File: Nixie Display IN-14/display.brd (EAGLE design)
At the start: 112.6 x 51.6 mm, 22 parts, among them U1 TPIC6B595DWRG4, U2 TPIC6B595DWRG4, U3 TPIC6B595DWRG4, U4 TPIC6B595DWRG4, U5 TPIC6B595DWRG4, X1 22-23-2021

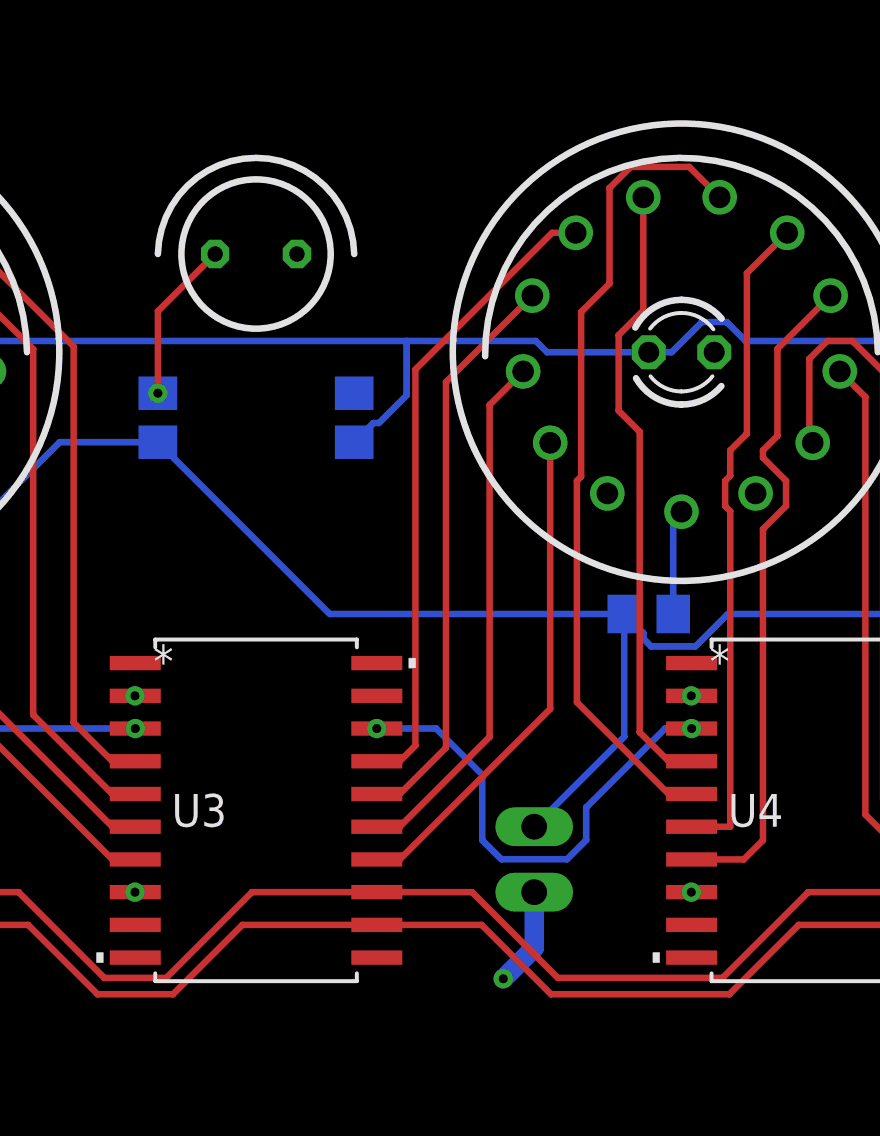
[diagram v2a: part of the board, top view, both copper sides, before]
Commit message: Reverses polarity of IN3
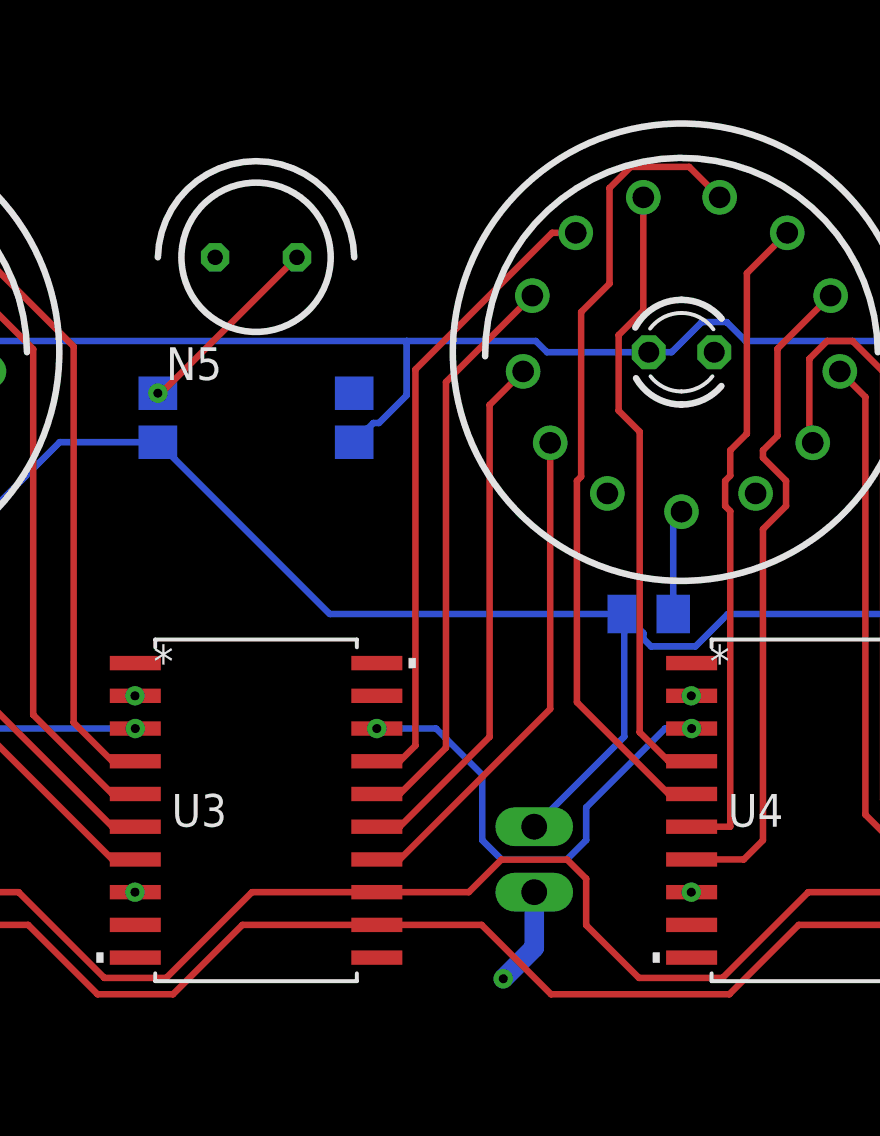
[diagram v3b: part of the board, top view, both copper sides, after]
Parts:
- moved N5 0.13 mm to (56.3, 38.1)
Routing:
- net N$49: track 109.0 -> 111.1 mm
- net N$22: track 6.32 -> 7.58 mm
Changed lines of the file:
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@@
 <setting verticaltext="up"/>
 </settings>
-<grid distance="5" unitdist="mil" unit="mil" style="lines" multiple="1" display="no" altdistance="5" altunitdist="mil" altunit="mil"/>
+<grid distance="50" unitdist="mil" unit="mil" style="lines" multiple="1" display="no" altdistance="5" altunitdist="mil" altunit="mil"/>
 <layers>
 <layer number="1" name="Top" color="4" fill="1" visible="yes" active="yes"/>
@@
 <element name="N3" library="nixies-us" package="IN-14" value="IN-14" x="72.771" y="34.417" smashed="yes"/>
 <element name="N4" library="nixies-us" package="IN-14" value="IN-14" x="96.901" y="34.417" smashed="yes"/>
-<element name="N5" library="nixies-us" package="IN-3" value="IN-3" x="56.261" y="38.227" smashed="yes"/>
 <element name="LED1" library="led" library_urn="urn:adsk.eagle:library:259" package="LED3MM" package3d_urn="urn:adsk.eagle:package:15797/1" value="" x="15.621" y="34.417" smashed="yes">
 <attribute name="POPULARITY" value="97" x="15.621" y="34.417" size="1.778" layer="27" display="off"/>
@@
 <attribute name="VALUE" x="72.136" y="17.272" locked="yes" size="1.016" layer="28" ratio="10" rot="MR270"/>
 </element>
+<element name="N5" library="nixies-us" package="IN-3" value="IN-3" x="56.261" y="38.1" smashed="yes">
+<attribute name="NAME" x="52.7685" y="33.3375" size="1.27" layer="25"/>
+</element>
 </elements>
 <signals>
@@
 <contactref element="LED2" pad="K"/>
 <contactref element="LED1" pad="K"/>
-<contactref element="N5" pad="K"/>
 <polygon width="0.254" layer="1" spacing="0.3048" orphans="yes">
 <vertex x="0" y="51.435"/>
@@
 <via x="65.853971875" y="10.100971875" extent="1-16" drill="0.35"/>
 <wire x1="67.056" y1="11.303" x2="65.853971875" y2="10.100971875" width="0.762" layer="16"/>
+<contactref element="N5" pad="K"/>
 </signal>
 <signal name="VCC">
@@
 <wire x1="62.103" y1="32.74058125" x2="62.103" y2="34.8529" width="0.254" layer="16"/>
 </signal>
-<signal name="N$22">
-<contactref element="N5" pad="A"/>
-<contactref element="R2" pad="2"/>
-<via x="52.451" y="32.827" extent="1-16" drill="0.35"/>
-<wire x1="52.451" y1="32.827" x2="52.451" y2="36.0045" width="0.254" layer="1"/>
-<wire x1="52.451" y1="36.0045" x2="54.6735" y2="38.227" width="0.254" layer="1"/>
-</signal>
 <signal name="N$23">
 <contactref element="N1" pad="A"/>
@@
 <via x="60.9473" y="19.812" extent="1-16" drill="0.35"/>
 <via x="73.1647" y="19.812" extent="1-16" drill="0.35"/>
-<wire x1="60.9473" y1="19.812" x2="63.246" y2="19.812" width="0.254" layer="16"/>
-<wire x1="63.246" y1="19.812" x2="63.24725625" y2="19.812" width="0.254" layer="16"/>
 <wire x1="72.13474375" y1="19.812" x2="73.1647" y2="19.812" width="0.254" layer="16"/>
 <wire x1="69.072" y1="16.74925625" x2="72.13474375" y2="19.812" width="0.254" layer="16"/>
-<wire x1="63.246" y1="19.812" x2="65.04" y2="18.018" width="0.254" layer="16"/>
 <wire x1="65.04" y1="15.47925625" x2="65.77925625" y2="14.74" width="0.254" layer="16"/>
 <wire x1="65.77925625" y1="14.74" x2="68.33274375" y2="14.74" width="0.254" layer="16"/>
@@
 <wire x1="65.04" y1="18.018" x2="65.04" y2="15.47925625" width="0.254" layer="16"/>
 <wire x1="69.072" y1="15.47925625" x2="69.072" y2="16.74925625" width="0.254" layer="16"/>
+<wire x1="60.9473" y1="19.812" x2="63.246" y2="19.812" width="0.254" layer="16"/>
+<wire x1="63.246" y1="19.812" x2="65.04" y2="18.018" width="0.254" layer="16"/>
 </signal>
 <signal name="N$27">
@@
 <wire x1="16.637" y1="3.81" x2="17.018" y2="4.191" width="0.254" layer="1"/>
 <wire x1="17.018" y1="9.68288125" x2="16.2687" y2="10.43218125" width="0.254" layer="1"/>
+<wire x1="67.708625" y1="9.4996" x2="74.62875" y2="9.4996" width="0.254" layer="1"/>
 <wire x1="60.9473" y1="12.192" x2="65.016225" y2="12.192" width="0.254" layer="1"/>
 <wire x1="65.016225" y1="12.192" x2="67.708625" y2="9.4996" width="0.254" layer="1"/>
-<wire x1="67.708625" y1="9.4996" x2="74.62875" y2="9.4996" width="0.254" layer="1"/>
 </signal>
 <signal name="N$49">
@@
 <wire x1="14.478" y1="10.89111875" x2="14.478" y2="4.191" width="0.254" layer="1"/>
 <wire x1="14.478" y1="4.191" x2="14.097" y2="3.81" width="0.254" layer="1"/>
-<wire x1="60.9473" y1="13.462" x2="64.64425625" y2="13.462" width="0.254" layer="1"/>
-<wire x1="64.64425625" y1="13.462" x2="67.97165625" y2="10.1346" width="0.254" layer="1"/>
-<wire x1="67.97165625" y1="10.1346" x2="74.36571875" y2="10.1346" width="0.254" layer="1"/>
+<wire x1="71.12" y1="10.1346" x2="74.36571875" y2="10.1346" width="0.254" layer="1"/>
+<wire x1="65.77925625" y1="14.724" x2="68.33274375" y2="14.724" width="0.254" layer="1"/>
+<wire x1="68.33274375" y1="14.724" x2="69.072" y2="13.98474375" width="0.254" layer="1"/>
+<wire x1="60.9473" y1="13.462" x2="64.51725625" y2="13.462" width="0.254" layer="1"/>
+<wire x1="69.072" y1="12.1826" x2="71.12" y2="10.1346" width="0.254" layer="1"/>
+<wire x1="64.51725625" y1="13.462" x2="65.77925625" y2="14.724" width="0.254" layer="1"/>
+<wire x1="69.072" y1="13.98474375" x2="69.072" y2="12.1826" width="0.254" layer="1"/>
 </signal>
 <signal name="N$52">
@@
 <wire x1="94.7547" y1="18.542" x2="93.863896875" y2="18.542" width="0.254" layer="1"/>
 </signal>
+<signal name="N$22">
+<contactref element="R2" pad="2"/>
+<contactref element="N5" pad="A"/>
+<wire x1="57.8485" y1="38.1" x2="52.5755" y2="32.827" width="0.254" layer="1"/>
+<wire x1="52.5755" y1="32.827" x2="52.451" y2="32.827" width="0.254" layer="1"/>
+<via x="52.451" y="32.827" extent="1-16" drill="0.35"/>
+</signal>
 </signals>
